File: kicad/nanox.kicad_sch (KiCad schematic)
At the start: 137 parts, among them P1 likely an ESD protection diod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, P2 likely an ESD protection diod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, P3 likely an ESD protection diod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, P4 likely an ESD protection diod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, P5 likely an ESD protection diod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, SW1 push button, left, SW2 push button, right, X1 ?, X10 unknown, marked 1C4F, likely 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, X2 unknown, marked 2GC, X3 unknown, marked 6, X4 ?, X5 ?, X6 ?, X7 ?, X8 ?, X9 unknown, marked P8W 26, Y1 crystal, likely the 32 MHz HSE

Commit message: Identify X10 as a TI TLV61046A, the OLED's boost converter
Its 1C4F marking is TI's marking for the TLV61046A, a 28 V boost converter
made for PMOLED panels, confirming that X10 makes the display's panel
supply. GND and the feedback divider fix its orientation, so its pads are
now named with their pins: VIN (6) on the supply X9 switches from battery
+, EN (4) on the +3.3V rail, VOUT (5) the OLED VCC to BTB pin 12, FB (3)
the R25/R26 divider and SW (1) the L1 inductor. OLED VCC and its feedback
lose their question marks; the switch node is named. Connectivity is
unchanged.

Co-Authored-By: Claude Opus 5.5 <noreply@anthropic.com>
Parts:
- TP38: value OLED VCC? -> OLED VCC
- X10: value unknown, marked 1C4F, likely the boost converter for the OLED panel supply -> TI TLV61046A boost converter (marked 1C4F)
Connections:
- net Net-T13 renamed OLED boost SW
- net OLED VCC feedback? renamed OLED VCC feedback
- net OLED VCC? renamed OLED VCC
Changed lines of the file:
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@@
  (label "OLED IREF?" (at 25.40 82.55 180) (effects (font (size 1.0 1.0)) (justify right bottom)))
  (label "+3.3V rail" (at 45.72 59.69 0) (effects (font (size 1.0 1.0)) (justify left bottom)))
- (label "OLED VCC?" (at 45.72 62.23 0) (effects (font (size 1.0 1.0)) (justify left bottom)))
+ (label "OLED VCC" (at 45.72 62.23 0) (effects (font (size 1.0 1.0)) (justify left bottom)))
  (no_connect (at 45.72 64.77))
  (no_connect (at 45.72 67.31))
@@
  )
  (label "GND" (at 76.20 73.66 180) (effects (font (size 1.0 1.0)) (justify right bottom)))
- (label "OLED VCC?" (at 96.52 73.66 0) (effects (font (size 1.0 1.0)) (justify left bottom)))
+ (label "OLED VCC" (at 96.52 73.66 0) (effects (font (size 1.0 1.0)) (justify left bottom)))
  (symbol (lib_id "nanox:C29") (at 86.36 88.90 0) (unit 1) (in_bom yes) (on_board yes) (dnp no)
   (property "Reference" "C29" (at 86.36 85.09 0) (effects (font (size 1.27 1.27))))
@@
   (instances (project "nanox" (path "/9fc871f3-1e36-5a01-9359-e2a20c86f96f" (reference "C33") (unit 1))))
  )
- (label "OLED VCC?" (at 76.20 165.10 180) (effects (font (size 1.0 1.0)) (justify right bottom)))
+ (label "OLED VCC" (at 76.20 165.10 180) (effects (font (size 1.0 1.0)) (justify right bottom)))
  (label "GND" (at 96.52 165.10 0) (effects (font (size 1.0 1.0)) (justify left bottom)))
  (symbol (lib_id "nanox:C34") (at 86.36 180.34 0) (unit 1) (in_bom yes) (on_board yes) (dnp no)
@@
   (instances (project "nanox" (path "/9fc871f3-1e36-5a01-9359-e2a20c86f96f" (reference "C34") (unit 1))))
  )
- (label "OLED VCC?" (at 76.20 180.34 180) (effects (font (size 1.0 1.0)) (justify right bottom)))
+ (label "OLED VCC" (at 76.20 180.34 180) (effects (font (size 1.0 1.0)) (justify right bottom)))
  (label "GND" (at 96.52 180.34 0) (effects (font (size 1.0 1.0)) (justify left bottom)))
  (symbol (lib_id "nanox:C35") (at 86.36 195.58 0) (unit 1) (in_bom yes) (on_board yes) (dnp no)
@@
   (instances (project "nanox" (path "/9fc871f3-1e36-5a01-9359-e2a20c86f96f" (reference "R25") (unit 1))))
  )
- (label "OLED VCC?" (at 185.42 256.54 180) (effects (font (size 1.0 1.0)) (justify right bottom)))
- (label "OLED VCC feedback?" (at 205.74 256.54 0) (effects (font (size 1.0 1.0)) (justify left bottom)))
+ (label "OLED VCC" (at 185.42 256.54 180) (effects (font (size 1.0 1.0)) (justify right bottom)))
+ (label "OLED VCC feedback" (at 205.74 256.54 0) (effects (font (size 1.0 1.0)) (justify left bottom)))
  (symbol (lib_id "nanox:R26") (at 195.58 271.78 0) (unit 1) (in_bom yes) (on_board yes) (dnp no)
   (property "Reference" "R26" (at 195.58 267.97 0) (effects (font (size 1.27 1.27))))
@@
   (instances (project "nanox" (path "/9fc871f3-1e36-5a01-9359-e2a20c86f96f" (reference "R26") (unit 1))))
  )
- (label "OLED VCC feedback?" (at 185.42 271.78 180) (effects (font (size 1.0 1.0)) (justify right bottom)))
+ (label "OLED VCC feedback" (at 185.42 271.78 180) (effects (font (size 1.0 1.0)) (justify right bottom)))
  (label "GND" (at 205.74 271.78 0) (effects (font (size 1.0 1.0)) (justify left bottom)))
  (symbol (lib_id "nanox:R27") (at 195.58 287.02 0) (unit 1) (in_bom yes) (on_board yes) (dnp no)
@@
  (symbol (lib_id "nanox:TP38") (at 449.58 119.38 0) (unit 1) (in_bom yes) (on_board yes) (dnp no)
   (property "Reference" "TP38" (at 449.58 115.57 0) (effects (font (size 1.27 1.27))))
-  (property "Value" "OLED VCC?" (at 449.58 123.19 0) (effects (font (size 1.27 1.27))))
+  (property "Value" "OLED VCC" (at 449.58 123.19 0) (effects (font (size 1.27 1.27))))
   (property "Footprint" "" (at 449.58 119.38 0) (effects (font (size 1.27 1.27)) hide))
   (property "Description" "test pad" (at 449.58 119.38 0) (effects (font (size 1.27 1.27)) hide))
@@
   (instances (project "nanox" (path "/9fc871f3-1e36-5a01-9359-e2a20c86f96f" (reference "TP38") (unit 1))))
  )
- (label "OLED VCC?" (at 439.42 119.38 180) (effects (font (size 1.0 1.0)) (justify right bottom)))
+ (label "OLED VCC" (at 439.42 119.38 180) (effects (font (size 1.0 1.0)) (justify right bottom)))
  (symbol (lib_id "nanox:TP39") (at 449.58 134.62 0) (unit 1) (in_bom yes) (on_board yes) (dnp no)
   (property "Reference" "TP39" (at 449.58 130.81 0) (effects (font (size 1.27 1.27))))
@@
  (label "VBUS" (at 473.71 238.76 0) (effects (font (size 1.0 1.0)) (justify left bottom)))
  (label "GND" (at 473.71 241.30 0) (effects (font (size 1.0 1.0)) (justify left bottom)))
- (symbol (lib_id "nanox:X10") (at 449.58 261.62 0) (unit 1) (in_bom yes) (on_board yes) (dnp no)
-  (property "Reference" "X10" (at 449.58 255.27 0) (effects (font (size 1.27 1.27))))
-  (property "Value" "unknown, marked 1C4F, likely the boost converter for the OLED panel supply" (at 449.58 267.97 0) (effects (font (size 1.27 1.27))))
-  (property "Footprint" "" (at 449.58 261.62 0) (effects (font (size 1.27 1.27)) hide))
-  (property "Description" "6 terminals, SOT-23-6 style, ~1.5 x 2.7 mm body" (at 449.58 261.62 0) (effects (font (size 1.27 1.27)) hide))
+ (symbol (lib_id "nanox:X10") (at 452.12 261.62 0) (unit 1) (in_bom yes) (on_board yes) (dnp no)
+  (property "Reference" "X10" (at 452.12 255.27 0) (effects (font (size 1.27 1.27))))
+  (property "Value" "TI TLV61046A boost converter (marked 1C4F)" (at 452.12 267.97 0) (effects (font (size 1.27 1.27))))
+  (property "Footprint" "" (at 452.12 261.62 0) (effects (font (size 1.27 1.27)) hide))
+  (property "Description" "SOT23-6 (DBV), 2.9 x 1.6 mm" (at 452.12 261.62 0) (effects (font (size 1.27 1.27)) hide))
   (pin "L1")
   (pin "L2")
@@
   (instances (project "nanox" (path "/9fc871f3-1e36-5a01-9359-e2a20c86f96f" (reference "X10") (unit 1))))
  )
- (label "Left button power (pad 19)" (at 439.42 259.08 180) (effects (font (size 1.0 1.0)) (justify right bottom)))
- (label "OLED VCC?" (at 439.42 261.62 180) (effects (font (size 1.0 1.0)) (justify right bottom)))
- (label "+3.3V rail" (at 439.42 264.16 180) (effects (font (size 1.0 1.0)) (justify right bottom)))
- (label "Net-T13" (at 459.74 259.08 0) (effects (font (size 1.0 1.0)) (justify left bottom)))
- (label "GND" (at 459.74 261.62 0) (effects (font (size 1.0 1.0)) (justify left bottom)))
- (label "OLED VCC feedback?" (at 459.74 264.16 0) (effects (font (size 1.0 1.0)) (justify left bottom)))
+ (label "Left button power (pad 19)" (at 440.69 259.08 180) (effects (font (size 1.0 1.0)) (justify right bottom)))
+ (label "OLED VCC" (at 440.69 261.62 180) (effects (font (size 1.0 1.0)) (justify right bottom)))
+ (label "+3.3V rail" (at 440.69 264.16 180) (effects (font (size 1.0 1.0)) (justify right bottom)))
+ (label "OLED boost SW" (at 463.55 259.08 0) (effects (font (size 1.0 1.0)) (justify left bottom)))
+ (label "GND" (at 463.55 261.62 0) (effects (font (size 1.0 1.0)) (justify left bottom)))
+ (label "OLED VCC feedback" (at 463.55 264.16 0) (effects (font (size 1.0 1.0)) (justify left bottom)))
  (symbol (lib_id "nanox:X9") (at 449.58 279.40 0) (unit 1) (in_bom yes) (on_board yes) (dnp no)
   (property "Reference" "X9" (at 449.58 274.32 0) (effects (font (size 1.27 1.27))))

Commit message: Identify PWR1 as an ST L6924D Li-ion battery charger
Its datasheet pinout matches every traced connection with our pin 1:
VIN and VINSNS tied, VOPRG grounded (4.2 V), VOSNS on battery +, R14 on
IPRG and R8 on IEND setting the charge and end-of-charge currents, C37 on
VREF, R11 holding SD low, ST2 to the MCU, VPRE and IPRE floating. Its pins
and nets are named after it (charger input, ST1/ST2, TPRG, SD, TH, VREF,
IEND, IPRG), with test pads 07, 13, 15 and 18. X9 turns out to sit between
battery +, the charger input and the OLED boost's supply, so it is likely
a power-path part. Connectivity is unchanged.

Co-Authored-By: Claude Opus 5.5 <noreply@anthropic.com>
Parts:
- PWR1: value unknown -> ST L6924D Li-ion battery charger
- TP07: value Switched supply? -> Charger input?
- TP13: value PWR1 pin 12 -> Charger VREF
- TP15: value PWR1 to MCU PA2? -> Charger ST2
- TP18: value PWR1 pin 15 -> Charger IPRG
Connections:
- net Net-T37 renamed Charger IPRG
- net Net-T38 renamed Charger input?
- net Net-T61 renamed Charger ST2
- net Net-T64 renamed Charger VREF
- net Net-T66 renamed Charger TPRG
- net Net-T67 renamed Charger SD
- net Net-T68 renamed Charger TH
- net Net-T69 renamed Charger ST1
- net Net-T70 renamed Charger IEND
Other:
- moved on the sheet: TP07

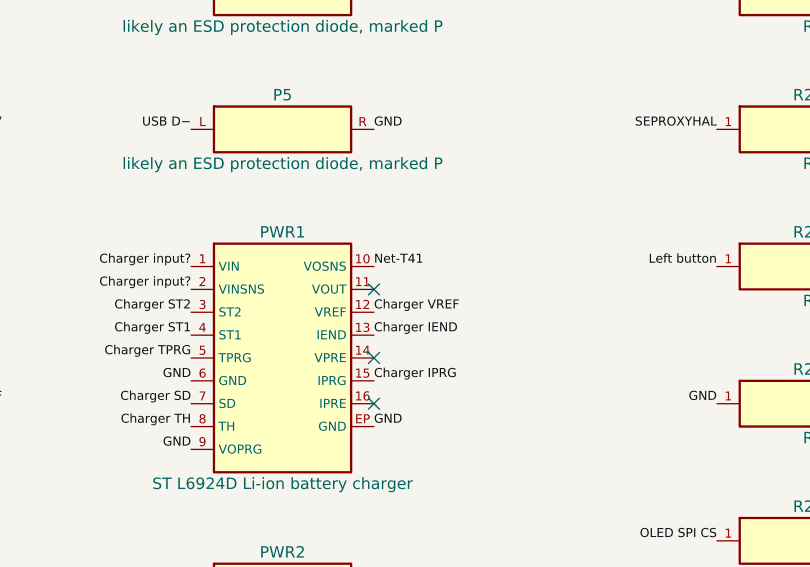
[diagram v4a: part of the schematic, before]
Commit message: Join the charger's VOUT and VOSNS pins on battery +
PWR1 pins 10 (VOSNS) and 11 (VOUT) are joined by copper running straight
between the two pads, so VOUT now reaches battery + too.

Co-Authored-By: Claude Opus 5.5 <noreply@anthropic.com>
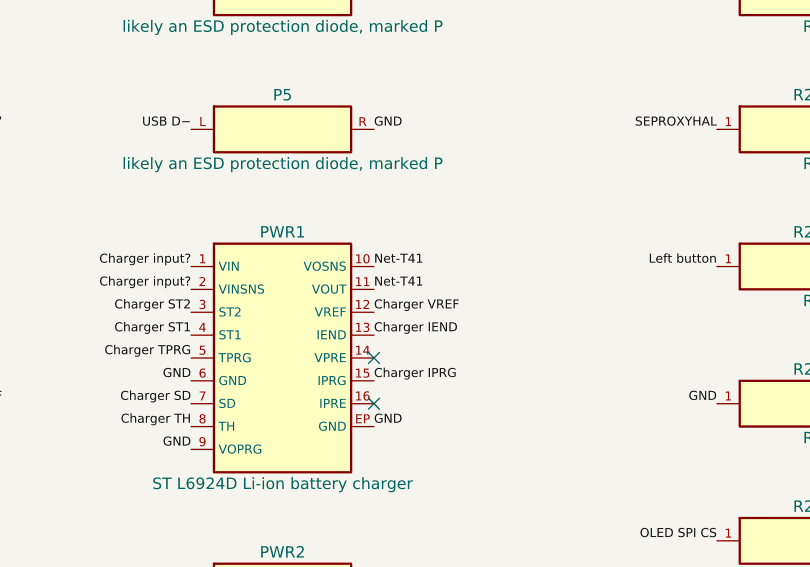
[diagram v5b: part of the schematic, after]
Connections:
- net Net-T41: now also PWR1.11 (VOUT)
- no-connect marks 79 -> 78
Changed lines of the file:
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@@
  (label "GND" (at 127.00 231.14 180) (effects (font (size 1.0 1.0)) (justify right bottom)))
  (label "Net-T41" (at 147.32 210.82 0) (effects (font (size 1.0 1.0)) (justify left bottom)))
- (no_connect (at 147.32 213.36))
+ (label "Net-T41" (at 147.32 213.36 0) (effects (font (size 1.0 1.0)) (justify left bottom)))
  (label "Charger VREF" (at 147.32 215.90 0) (effects (font (size 1.0 1.0)) (justify left bottom)))
  (label "Charger IEND" (at 147.32 218.44 0) (effects (font (size 1.0 1.0)) (justify left bottom)))

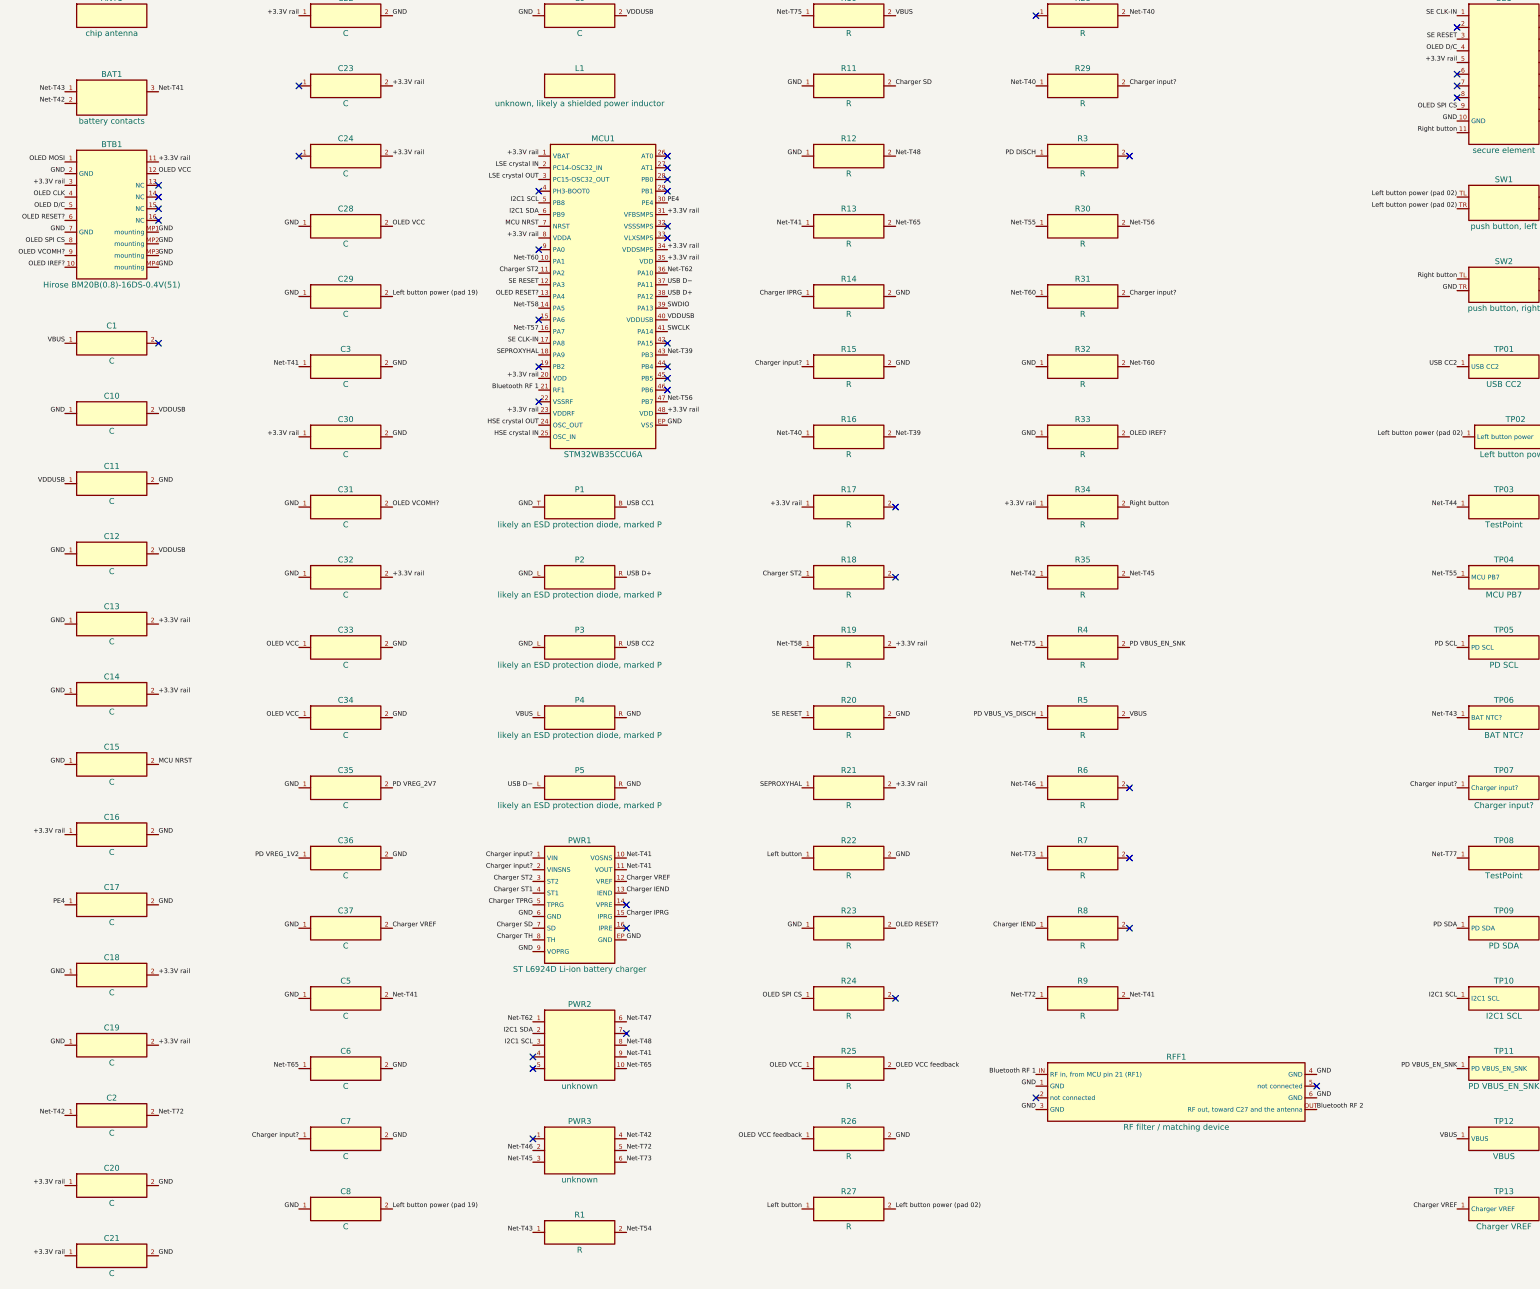
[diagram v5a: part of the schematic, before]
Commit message: Connect the charger's TH pin to the battery NTC through an inner layer
PWR1 pin 8 (TH) ends at a via with nothing on the back, and R1 leads to
another via with nothing on the back: they are joined on an inner layer
the photos can't show. TH now runs through it to R1 and on to the battery's
temperature sensor on battery pad 1 (named Battery NTC?, with TP06).

Paths can now be on the "inner" side: KiCad puts them on In2 (In1 is the
assumed ground plane), the photo viewer draws them dashed like a route on
the other side, and the 3D view leaves them inside the board. The inner
route is drawn only to make the connection; its real path isn't known.

Co-Authored-By: Claude Opus 5.5 <noreply@anthropic.com>
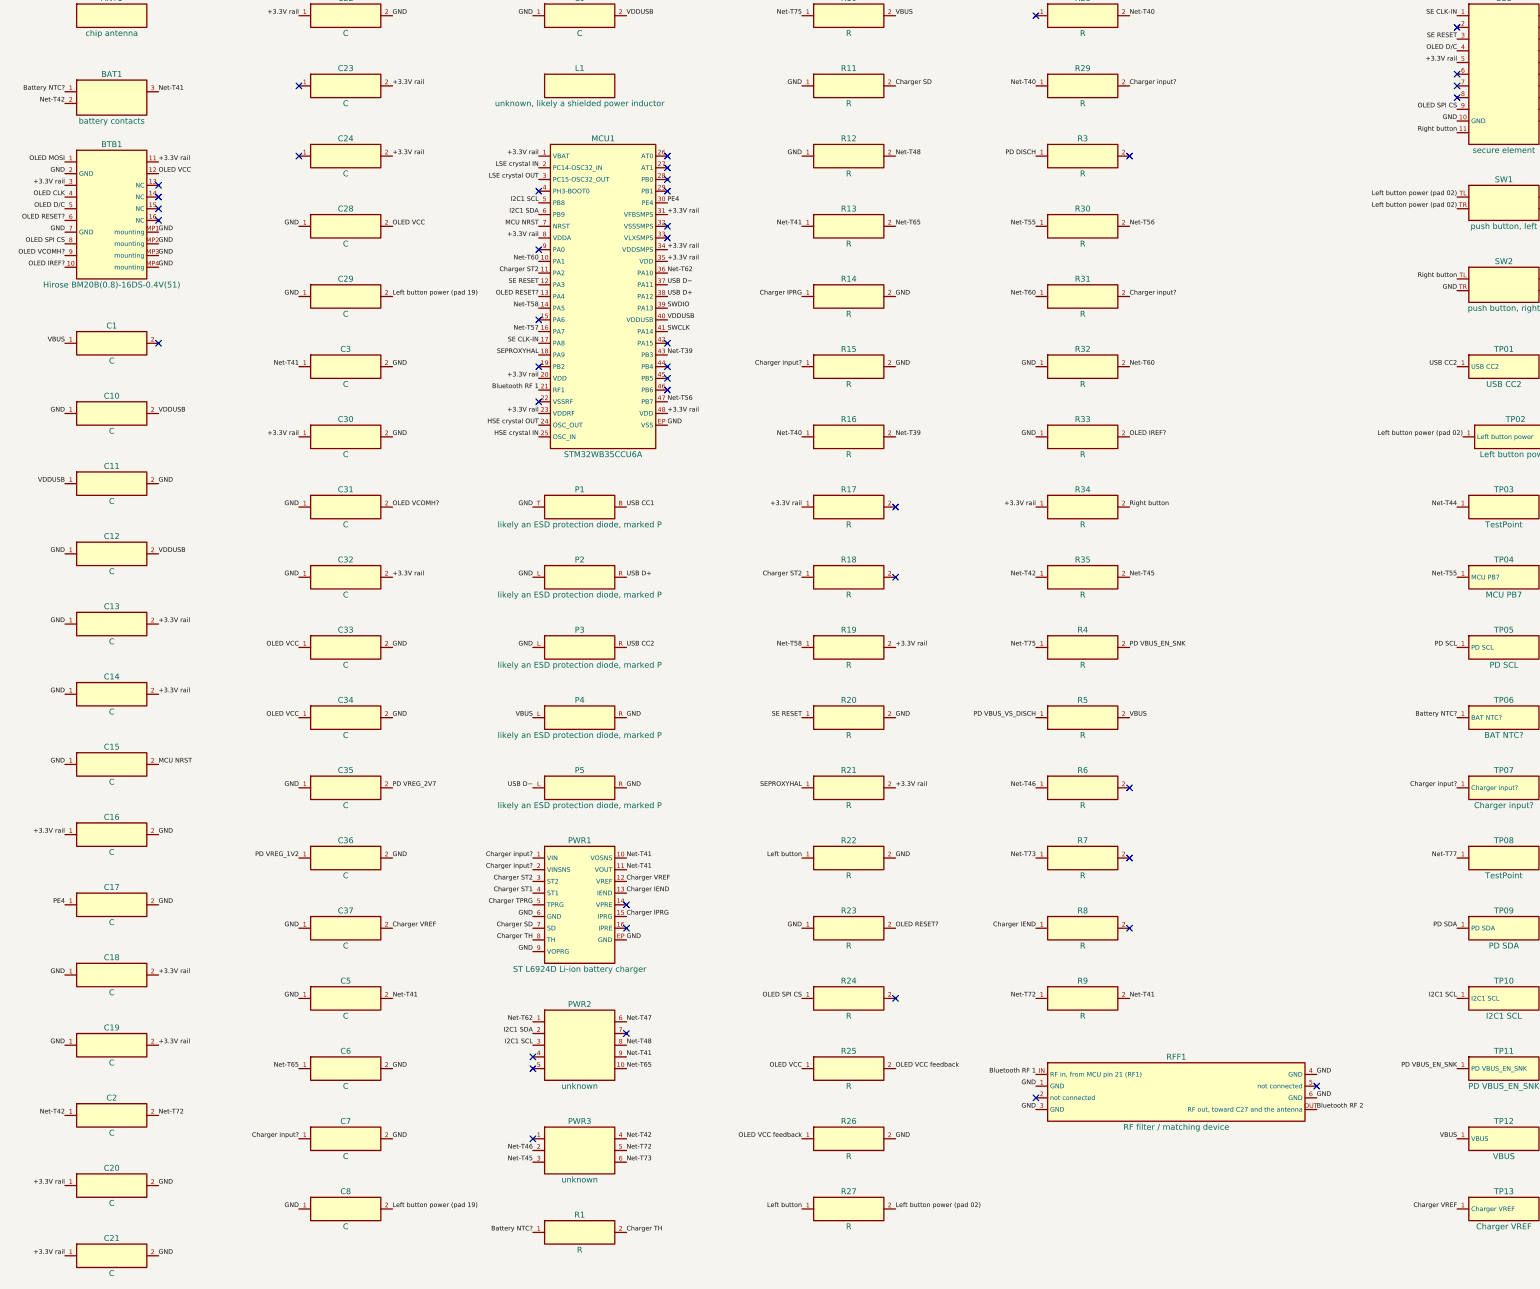
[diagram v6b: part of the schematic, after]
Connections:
- net Net-T54 is gone; now on net Charger TH: R1.2
- net Net-T43 renamed Battery NTC?
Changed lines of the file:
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@@
   (instances (project "nanox" (path "/9fc871f3-1e36-5a01-9359-e2a20c86f96f" (reference "BAT1") (unit 1))))
  )
- (label "Net-T43" (at 25.40 44.45 180) (effects (font (size 1.0 1.0)) (justify right bottom)))
+ (label "Battery NTC?" (at 25.40 44.45 180) (effects (font (size 1.0 1.0)) (justify right bottom)))
  (label "Net-T42" (at 25.40 46.99 180) (effects (font (size 1.0 1.0)) (justify right bottom)))
  (label "Net-T41" (at 45.72 44.45 0) (effects (font (size 1.0 1.0)) (justify left bottom)))
@@
   (instances (project "nanox" (path "/9fc871f3-1e36-5a01-9359-e2a20c86f96f" (reference "R1") (unit 1))))
  )
- (label "Net-T43" (at 127.00 292.10 180) (effects (font (size 1.0 1.0)) (justify right bottom)))
- (label "Net-T54" (at 147.32 292.10 0) (effects (font (size 1.0 1.0)) (justify left bottom)))
+ (label "Battery NTC?" (at 127.00 292.10 180) (effects (font (size 1.0 1.0)) (justify right bottom)))
+ (label "Charger TH" (at 147.32 292.10 0) (effects (font (size 1.0 1.0)) (justify left bottom)))
  (symbol (lib_id "nanox:R10") (at 195.58 27.94 0) (unit 1) (in_bom yes) (on_board yes) (dnp no)
   (property "Reference" "R10" (at 195.58 24.13 0) (effects (font (size 1.27 1.27))))
@@
   (instances (project "nanox" (path "/9fc871f3-1e36-5a01-9359-e2a20c86f96f" (reference "TP06") (unit 1))))
  )
- (label "Net-T43" (at 327.66 180.34 180) (effects (font (size 1.0 1.0)) (justify right bottom)))
+ (label "Battery NTC?" (at 327.66 180.34 180) (effects (font (size 1.0 1.0)) (justify right bottom)))
  (symbol (lib_id "nanox:TP07") (at 337.82 195.58 0) (unit 1) (in_bom yes) (on_board yes) (dnp no)
   (property "Reference" "TP07" (at 337.82 191.77 0) (effects (font (size 1.27 1.27))))
